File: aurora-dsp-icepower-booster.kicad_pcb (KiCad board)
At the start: 2 copper layers, 200 x 200 mm, 243 parts, among them J1 XLR_IN_1, J10 XLR3_OUT, J11 XLR3_OUT, J12 XLR3_OUT, J13 24V DC, J14 REMOTE 3.5mm, J2 XLR_IN_2, J3 XLR_IN_3, J4 XLR_IN_4, J5 XLR_IN_5, J6 XLR_IN_6, J7 XLR3_OUT, J8 XLR3_OUT, J9 XLR3_OUT, SW1 Gain CH1, SW2 Gain CH2, SW3 Gain CH3, SW4 Gain CH4, SW5 Gain CH5, SW6 Gain CH6, SW7 ALWAYS/REMOTE, U1 LM4562, U10 LM4562, U11 LM4562, U12 LM4562, U13 TEL5-2422, U14 ADP7118ARDZ-11, U15 ADP7182AUJZ-11, U2 LM4562, U3 LM4562, U4 LM4562, U5 LM4562, U6 LM4562, U7 LM4562, U8 LM4562, U9 LM4562

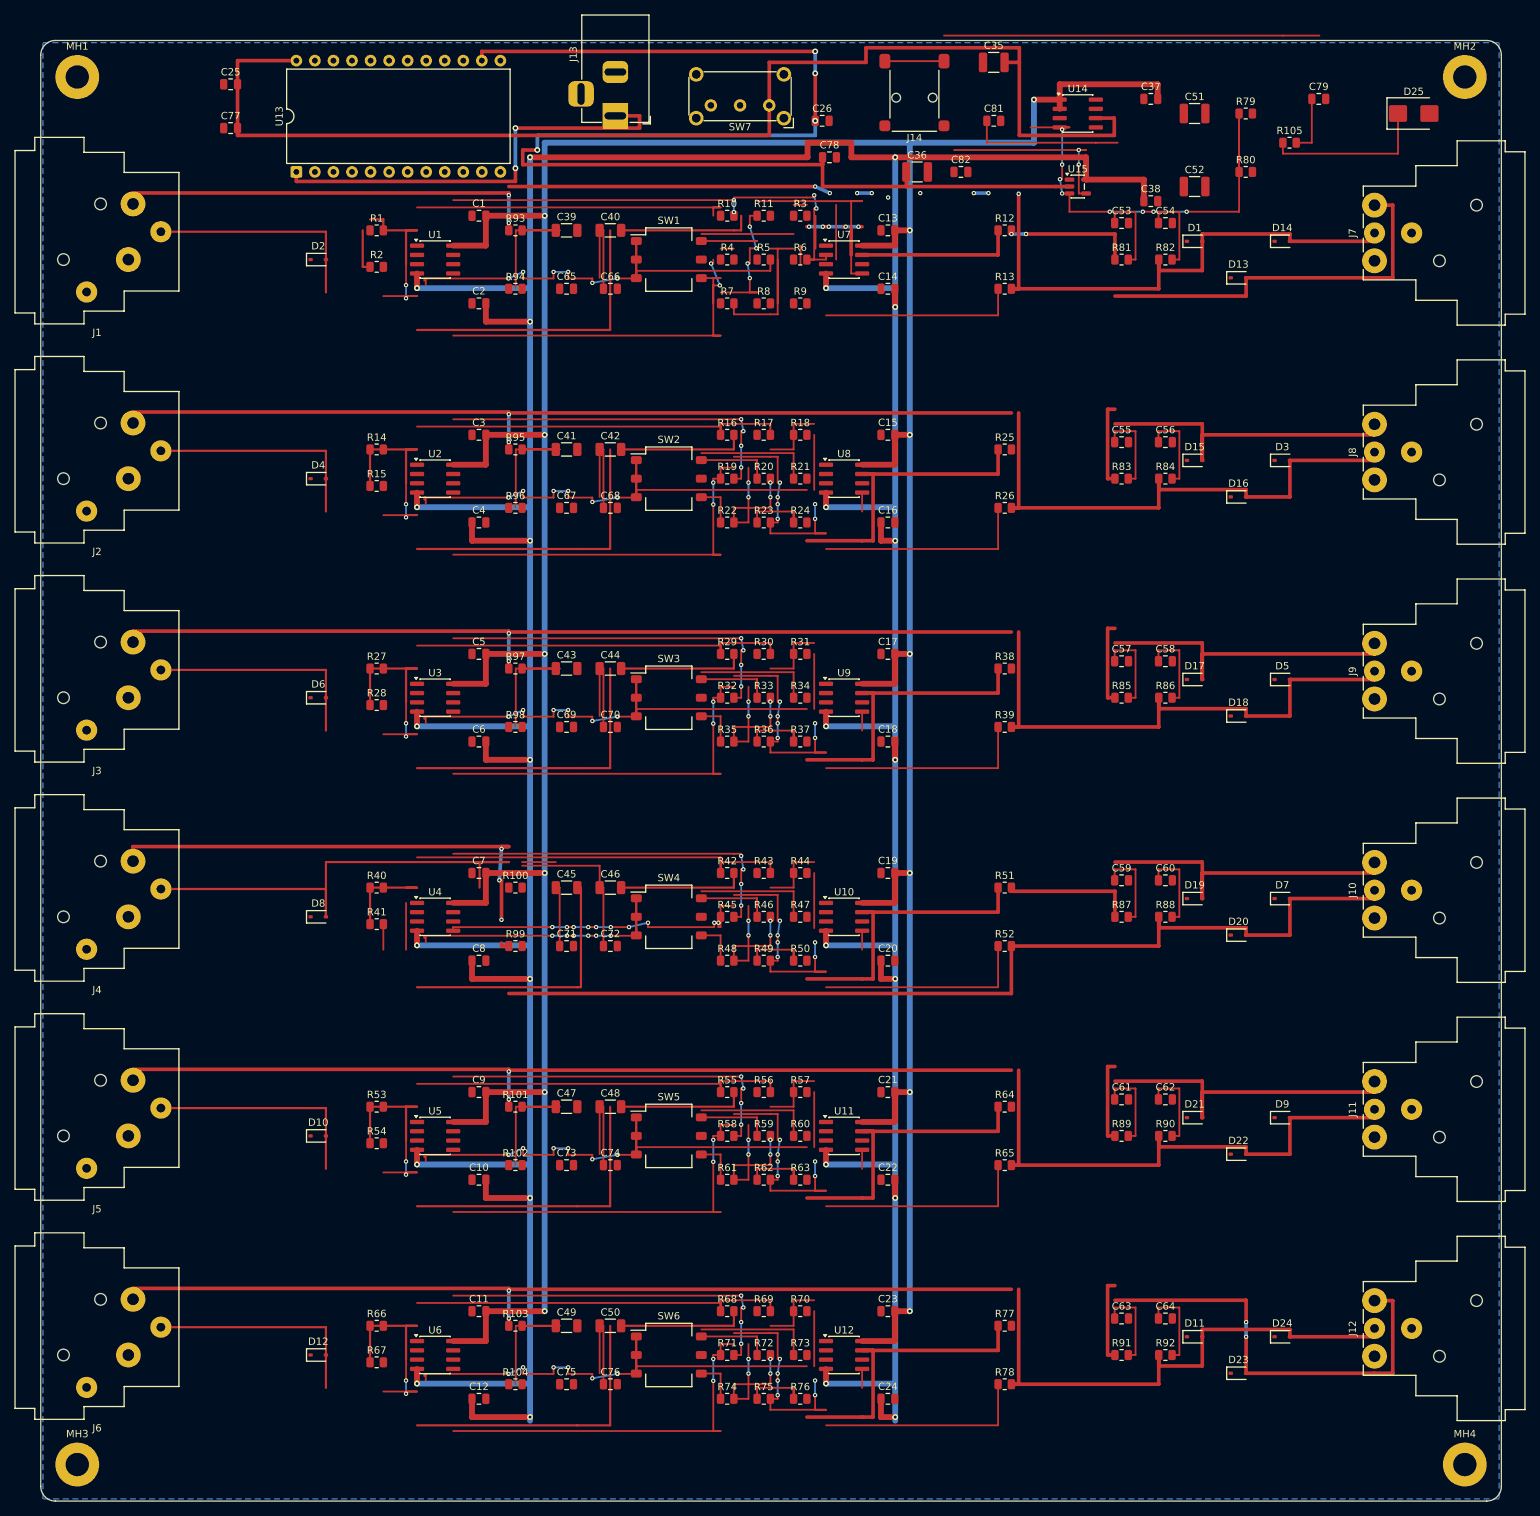
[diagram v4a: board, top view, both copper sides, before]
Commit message: Phase 4: 49 signal gaps geroutet, 0 errors (259 unconnected verbleiben)
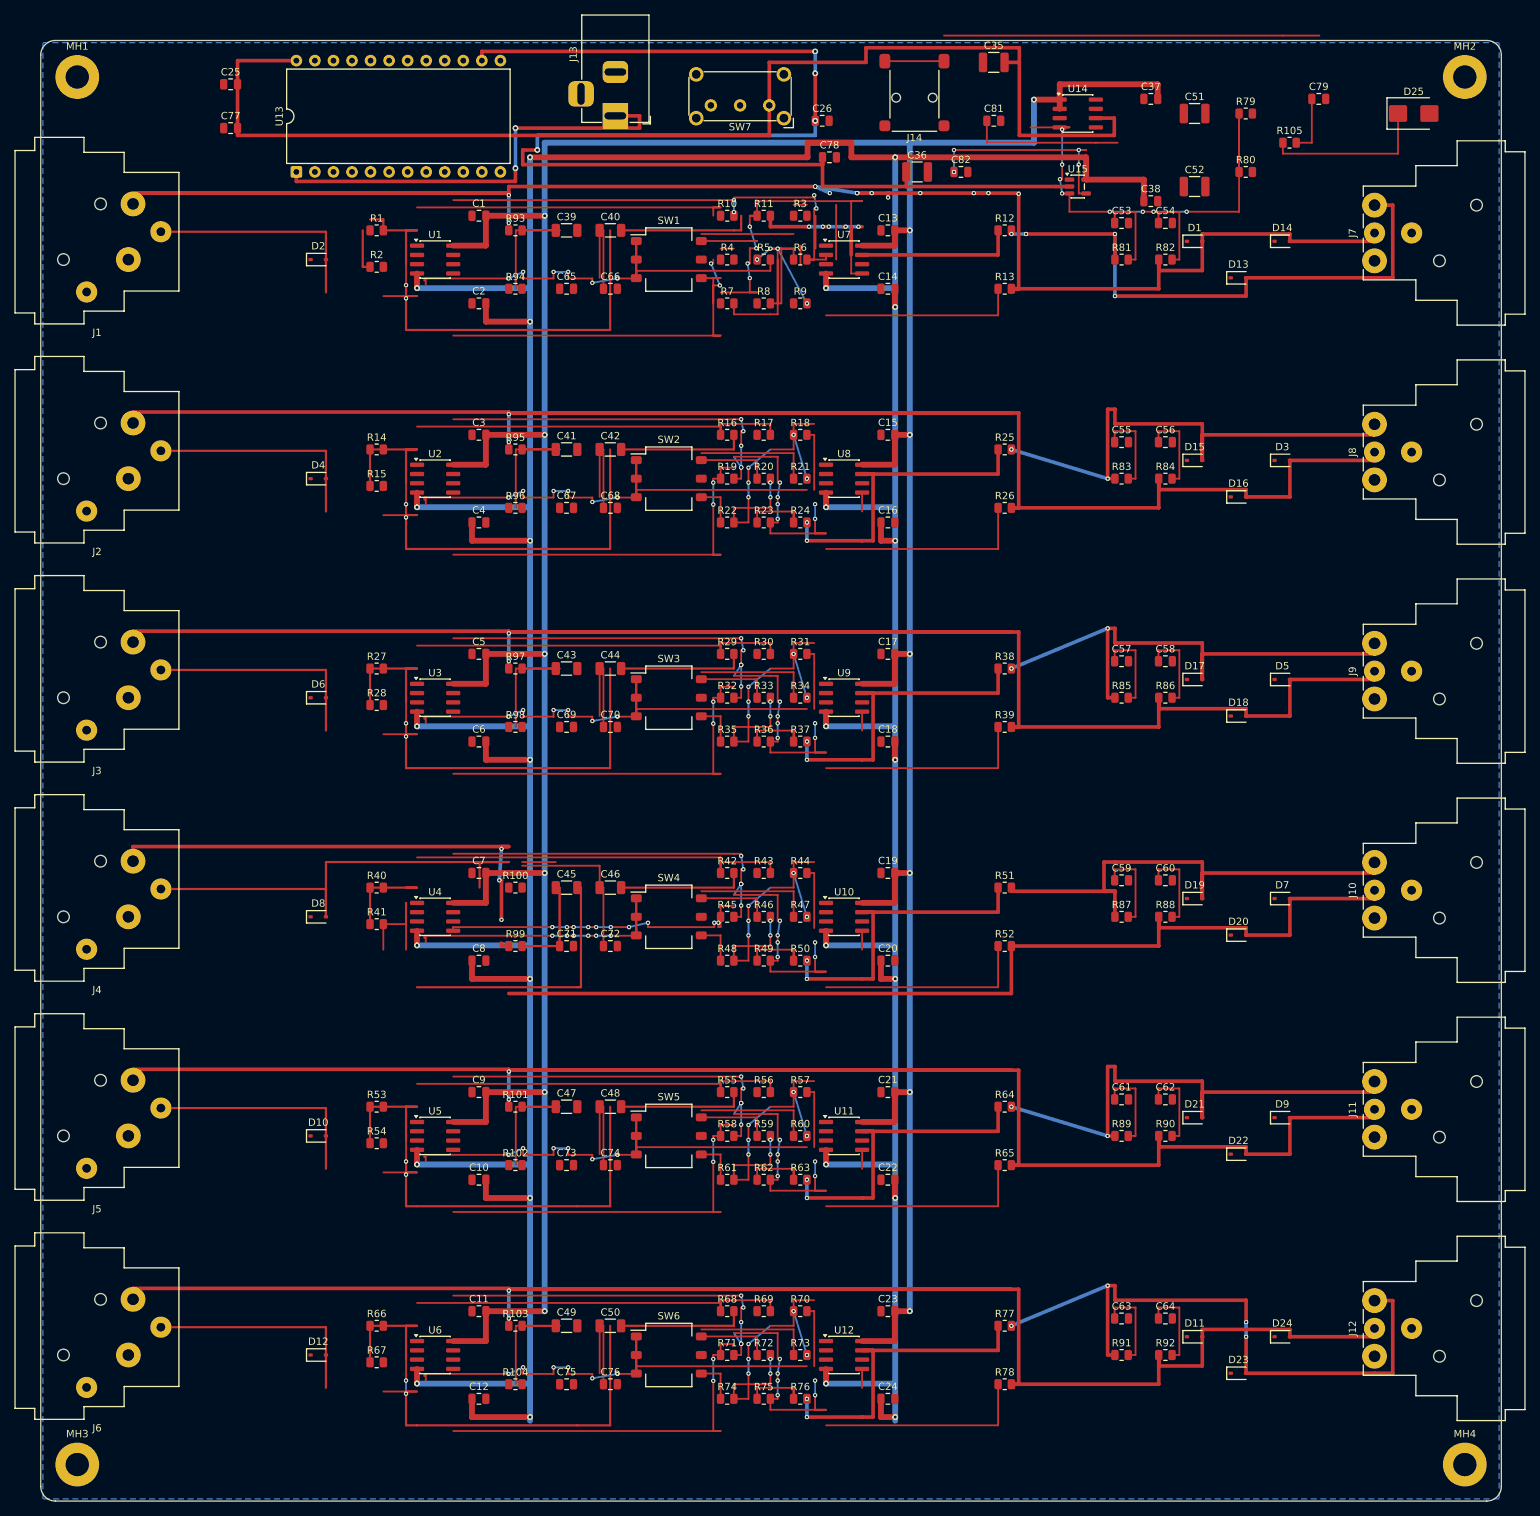
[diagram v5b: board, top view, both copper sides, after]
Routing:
- net /CH1_OUT_COLD: track 182.7 -> 264.2 mm, vias 11 -> 13
- net /CH6_OUT_COLD: track 203.3 -> 273.1 mm
- net /CH5_OUT_COLD: track 203.3 -> 273.1 mm
- net /CH3_OUT_COLD: track 203.3 -> 273.1 mm
- net /CH2_OUT_COLD: track 203.3 -> 273.1 mm
- net /CH1_SUMNODE: track 36.8 -> 61.9 mm, vias 0 -> 4
- net /CH6_OUT_HOT: track 72.0 -> 88.3 mm, vias 2 -> 4
- net /CH3_OUT_HOT: track 57.0 -> 73.3 mm, vias 0 -> 2
- net /CH5_OUT_HOT: track 57.0 -> 72.8 mm, vias 0 -> 2
- net /CH2_OUT_HOT: track 57.0 -> 72.8 mm, vias 0 -> 2
- net /CH4_EMI_HOT: track 13.1 -> 26.3 mm
- net /CH6_SUMNODE: track 82.3 -> 92.5 mm, vias 6 -> 9
- net /CH5_SUMNODE: track 82.3 -> 92.5 mm, vias 6 -> 9
- net /CH2_SUMNODE: track 82.3 -> 92.5 mm, vias 6 -> 9
- net /CH4_SUMNODE: track 73.7 -> 83.9 mm, vias 14 -> 17
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
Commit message: Phase 5b: GND copper pour + 112 GND vias, 0 errors, 129 unconnected
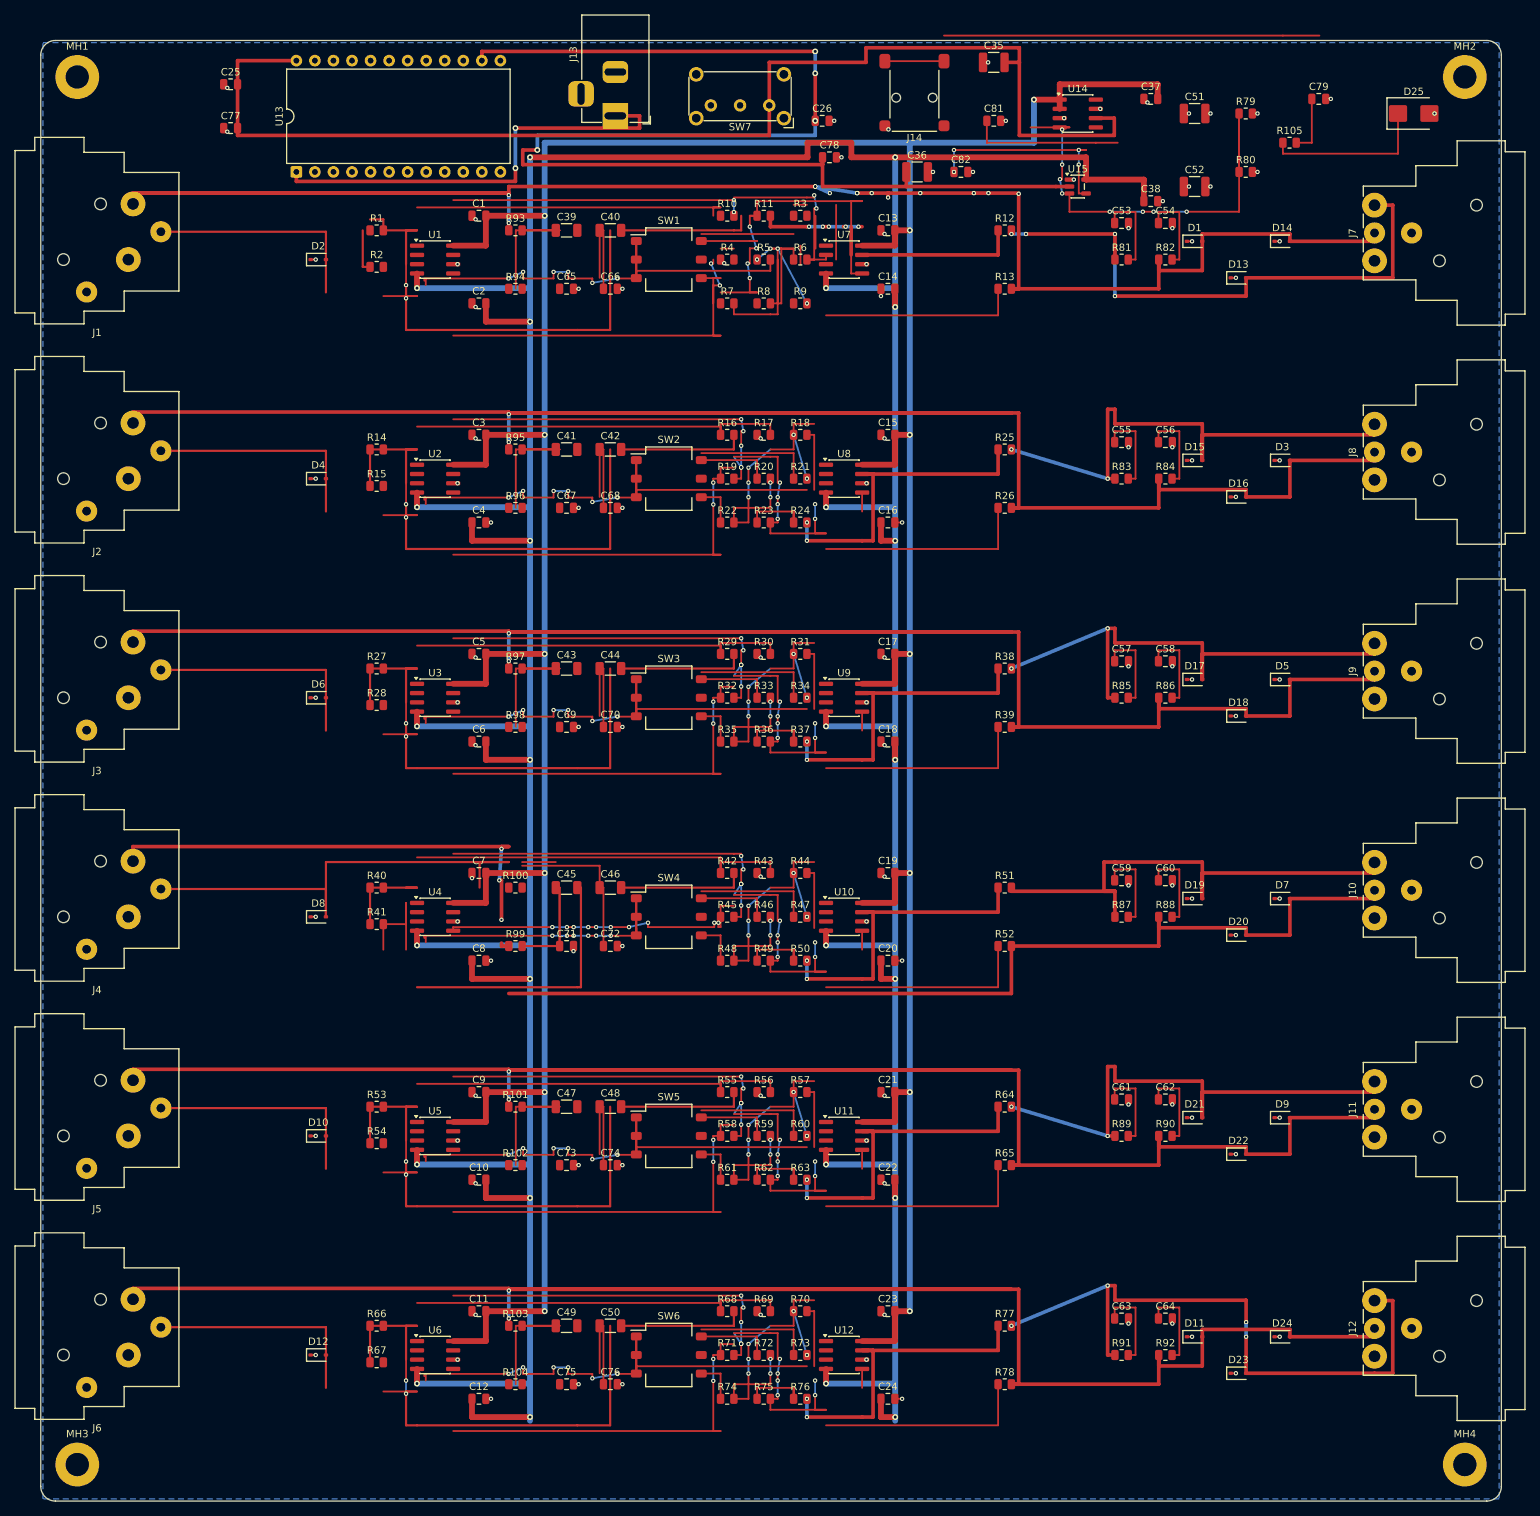
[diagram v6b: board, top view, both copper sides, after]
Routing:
- net /GND: track 0.00 -> 78.1 mm, vias 0 -> 112

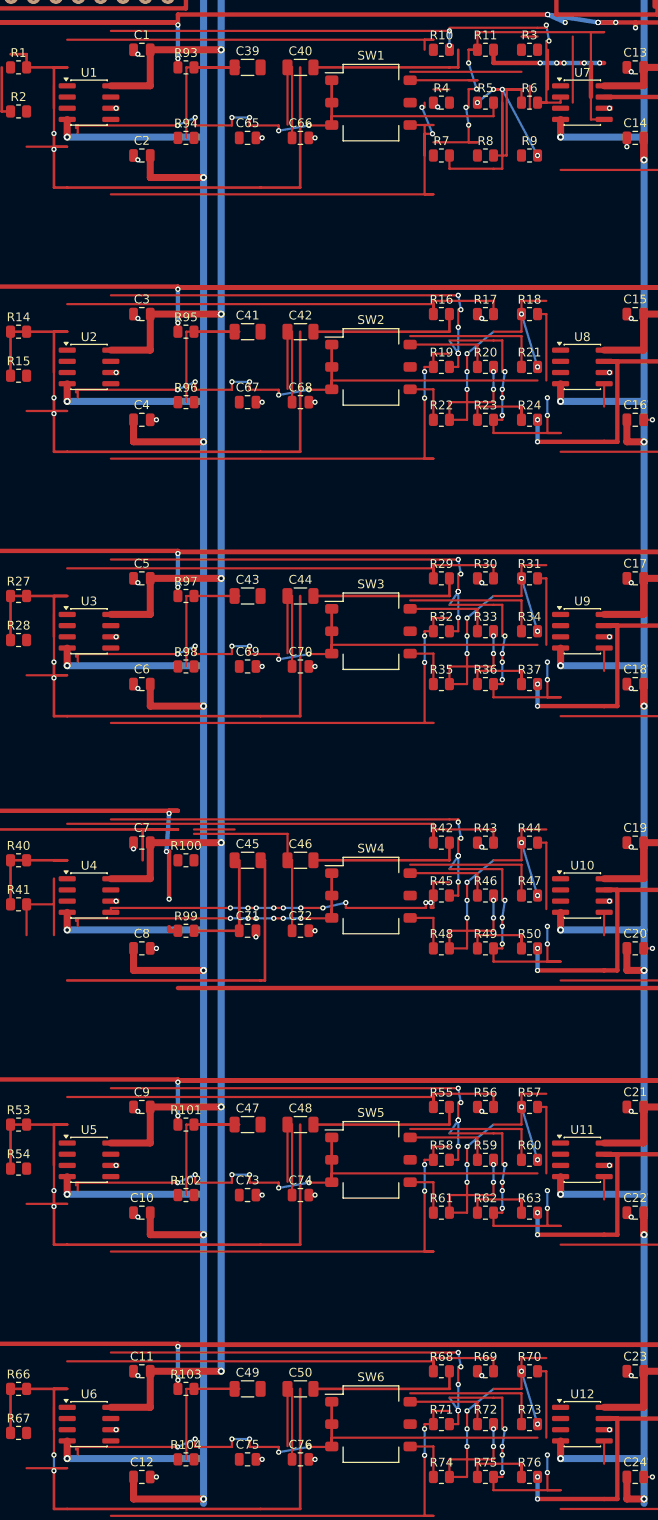
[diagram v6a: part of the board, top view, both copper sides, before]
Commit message: Phase 5c: Signal routing iterativ, 0 errors, 118 unconnected (2 GND + 116 Signal)
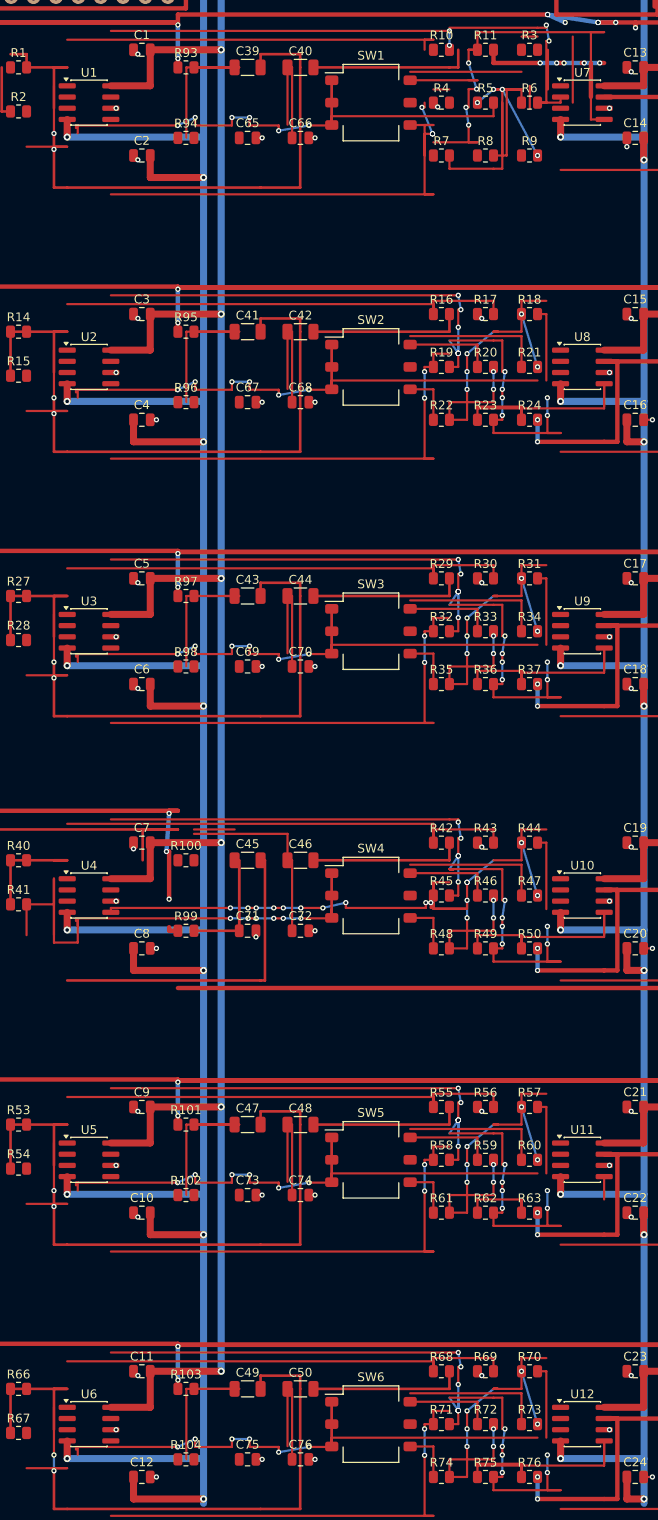
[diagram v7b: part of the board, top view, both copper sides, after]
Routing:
- net /CH2_GAIN_FB: track 12.1 -> 29.5 mm
- net /CH6_GAIN_FB: track 12.1 -> 29.5 mm
- net /CH4_RX_OUT: track 65.9 -> 78.6 mm
- net /CH4_GAIN_FB: track 12.1 -> 24.5 mm
- net /CH3_GAIN_FB: track 12.1 -> 24.5 mm
- net /CH4_SUMNODE: track 83.9 -> 95.5 mm, vias 17 -> 18
- net /CH6_HOT_IN: track 77.1 -> 84.6 mm
- net /CH5_HOT_IN: track 78.9 -> 86.4 mm
- net /CH3_HOT_IN: track 78.9 -> 86.4 mm
- net /CH1_HOT_IN: track 81.4 -> 88.9 mm
- net /CH2_HOT_IN: track 78.9 -> 86.4 mm
- net /CH5_GAIN_OUT: track 81.6 -> 86.1 mm, vias 11 -> 14
- net /CH6_GAIN_OUT: track 81.6 -> 86.0 mm, vias 11 -> 14
- net /CH4_GAIN_OUT: track 82.1 -> 84.6 mm
- net /CH3_SUMNODE: track 92.5 -> 94.5 mm
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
